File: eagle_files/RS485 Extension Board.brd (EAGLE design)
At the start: 100 x 80 mm, 4 parts, among them J1 RJ12 - 1, J2 RJ12 - 2, J3 RJ12 - 3, J4 RJ12 - 4

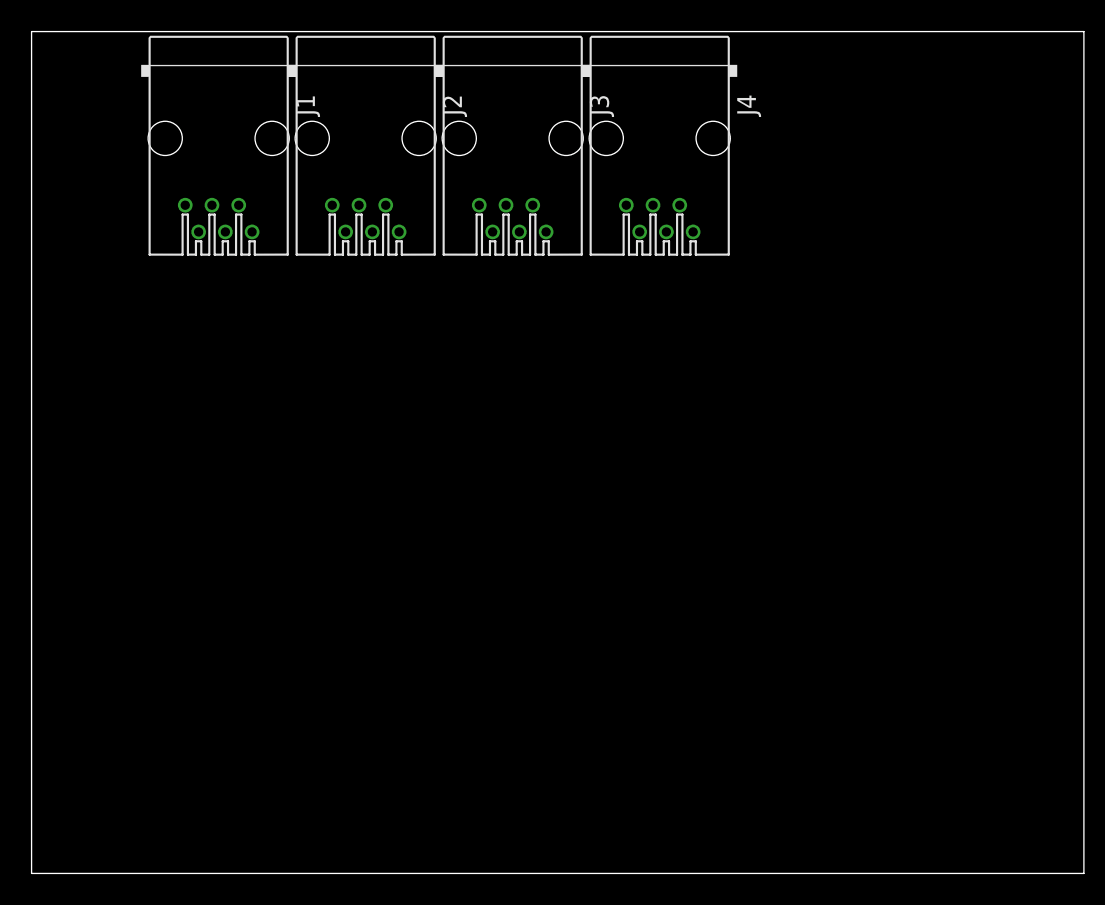
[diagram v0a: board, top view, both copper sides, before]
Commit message: add connector and ic
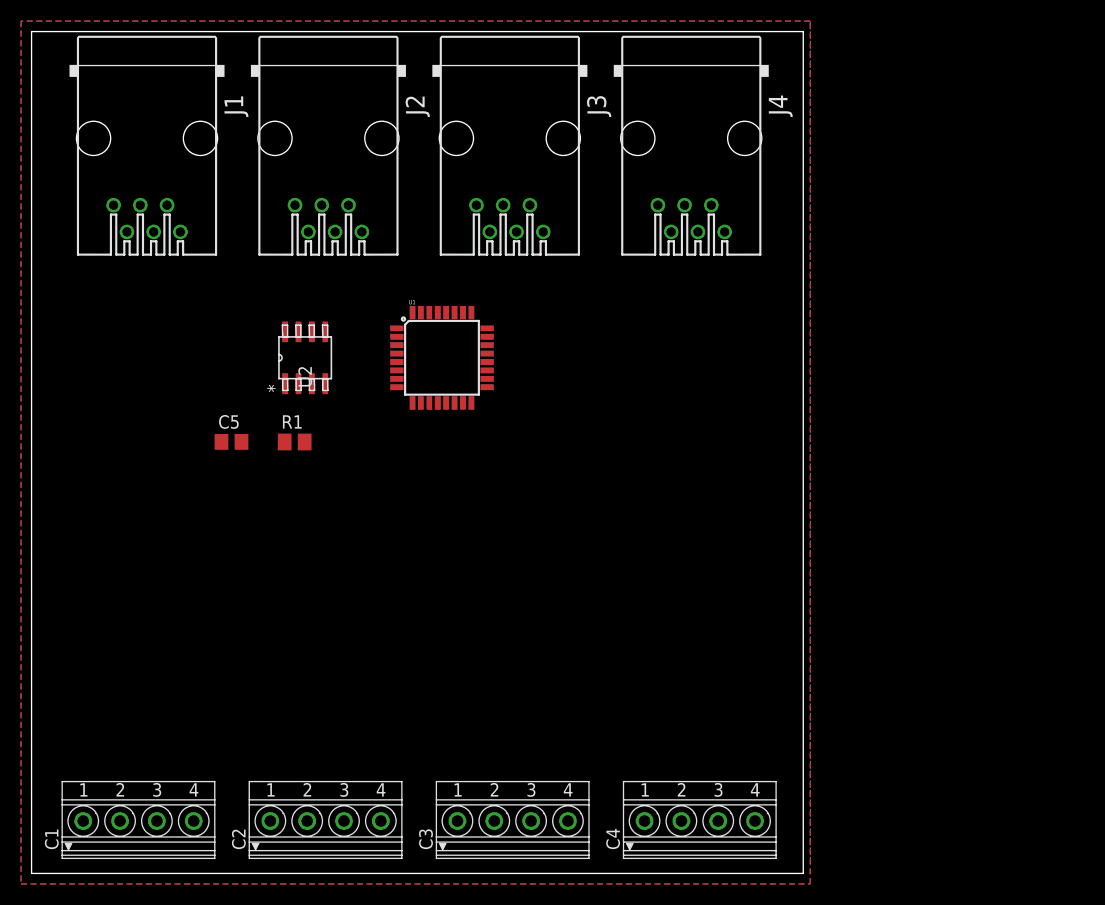
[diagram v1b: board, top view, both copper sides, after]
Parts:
- added C1, C2, C3, C4: 1751264, con-phoenix-350:1751264
- added C5: 100n, rcl:C0805
- added R1: 10u, rcl:M0805
- added U1: ATMEGA328P_TQFP, SparkFun-DigitalIC:TQFP32-08
- added U2: MAX3082ESA, MAX3082ESA:21-0041B_8
- moved J1 6.81 mm to (11.0, 69.8)
- moved J2 3.54 mm to (28.2, 69.8)
- moved J4 3.00 mm to (62.7, 69.8)
- moved J3 0.27 mm to (45.5, 69.8)
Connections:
- removed net N$3: J1.4
- removed net N$4: J1.5
- new net +12V: J1.2, J2.2, J3.2, J4.2
- new net +5V: C5.2, J1.3, J2.3, J3.3, J4.3, R1.1, U1.18, U1.4, U2.8
- new net GND: C1.4, C2.4, C3.4, C4.4, C5.1, J1.4, J2.4, J3.4, J4.4, U1.21, U1.3, U1.5, U2.5
- new net ONEWIRE: J1.5, J2.5, J3.5, J4.5
- new net RXD: U1.30, U2.1
- new net TXD: U1.31, U2.4
- net N$1: now also U2.2, U2.3; no longer J1.2
- net N$2: now also R1.2, U1.6; no longer J1.3
- net RS485-A: now also U2.6
- net RS485-B: now also U2.7
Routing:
- added copper zone on layer 1, net GND
- added copper zone on layer 16, net GND
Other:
- board size 100 x 80 mm -> 73.3 x 80 mm
